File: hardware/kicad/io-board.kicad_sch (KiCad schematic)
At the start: 50 parts, among them J1 NCJ6FI-S, J2 NCJ6FI-S, J3 NCJ6FI-S, J4 NCJ6FI-S, P1 JIO-PWR, P2 JIO-WETSEND, P3 JIO-WETRET, P4 JIO-DRY, P5 Wet/Dry control, P6 Mono switch, U1 OPA1644AIDR, U2 OPA1656IDR, U3 OPA1656IDR, U4 OPA1656IDR

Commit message: Board 6 io-board complete (ERC 0, sim verified, DRC 0/0 with ground grid stitching); all six boards READY TO ORDER; fab packet with gerber zips, BOMs, pos files, ORDER-PACKET.md; readiness report regenerated
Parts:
- removed C1, C2, C3, C4: 220p DNP, Capacitor_SMD:C_0603_1608Metric, symbol Device:C_Small
- removed C91, C92, C93, C94, C95, C96, C97, C98: 100n, Capacitor_SMD:C_0603_1608Metric, symbol Device:C_Small
- removed J1, J2, J3, J4: NCJ6FI-S, Connector_Audio:Jack_XLR-6.35mm_Neutrik_NCJ6FI-V_Vertical, symbol Connector_Audio:NCJ6FI-V
- removed R1, R2, R3, R4: 100R, Resistor_SMD:R_0603_1608Metric, symbol Device:R_Small
- removed R11, R12, R13, R14, R15, R16, R17, R18: 10k 0.1%, Resistor_SMD:R_0603_1608Metric, symbol Device:R_Small
- removed R31, R32, R35, R36: 20k, Resistor_SMD:R_0603_1608Metric, symbol Device:R_Small
- removed R43, R44, R53, R54: 10k, Resistor_SMD:R_0603_1608Metric, symbol Device:R_Small
- removed R49, R50, R59, R60: 49.9R, Resistor_SMD:R_0603_1608Metric, symbol Device:R_Small
- removed U1: OPA1644AIDR, Package_SO:SOIC-14_3.9x8.7mm_P1.27mm, symbol Amplifier_Operational:OPA4134
- added C1, C2, C3, C4: 220p, Capacitor_SMD:C_0805_2012Metric, symbol Device:C
- added C100, C99: 22u, Capacitor_SMD:C_1210_3225Metric, symbol Device:C
- added C91, C92, C93, C94, C95, C96, C97, C98: 100n, Capacitor_SMD:C_0805_2012Metric, symbol Device:C
- added J1: to L IN combo jack, Connector_JST:JST_XH_B3B-XH-A_1x03_P2.50mm_Vertical, symbol Connector_Generic:Conn_01x03
- added J2: to R IN combo jack, Connector_JST:JST_XH_B3B-XH-A_1x03_P2.50mm_Vertical, symbol Connector_Generic:Conn_01x03
- added J3: to L OUT combo jack, Connector_JST:JST_XH_B3B-XH-A_1x03_P2.50mm_Vertical, symbol Connector_Generic:Conn_01x03
- added J4: to R OUT combo jack, Connector_JST:JST_XH_B3B-XH-A_1x03_P2.50mm_Vertical, symbol Connector_Generic:Conn_01x03
- added R1, R2, R21, R22, R23, R24, R3, R4: 100, Resistor_SMD:R_0805_2012Metric, symbol Device:R
- added R11, R12, R13, R14, R15, R16, R17, R18, R43, R44, R53, R54: 10k, Resistor_SMD:R_0805_2012Metric, symbol Device:R
- added R31, R32, R35, R36: 20k, Resistor_SMD:R_0805_2012Metric, symbol Device:R
- added R49, R50, R59, R60: 49.9, Resistor_SMD:R_0805_2012Metric, symbol Device:R
- added U1: OPA1644AIDR, Package_SO:SOIC-14_3.9x8.7mm_P1.27mm, symbol Amplifier_Operational:TL074
- P1: value JIO-PWR -> JIO-PWR B3P-VH-B
- P2: value JIO-WETSEND -> P2
- P3: value JIO-WETRET -> P3
- P4: value JIO-DRY -> P4
- P5: value Wet/Dry control -> P5
- P6: value Mono switch -> P6
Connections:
- net +15VA: now also P1.1 (Pin_1), U2.8 (V+), U3.8 (V+), U4.8 (V+), C91.1, C93.1, C95.1, C97.1, C99.1, U1.4 (V+)
- net -15VA: now also P1.3 (Pin_3), U2.4 (V-), U3.4 (V-), U4.4 (V-), C100.1, C92.1, C94.1, C96.1, C98.1, U1.11 (V-)
- net AGND: now also P1.2 (Pin_2), P2.2 (Pin_2), P3.2 (Pin_2), P4.2 (Pin_2), U2.3 (+), U2.5 (+), U3.5 (+), U4.5 (+), C1.2, C100.2, C2.2, C3.2, C4.2, C91.2, C92.2, C93.2, C94.2, C95.2, C96.2, C97.2, C98.2, C99.2, J1.3 (Pin_3), J2.3 (Pin_3), J3.3 (Pin_3), J4.3 (Pin_3), R14.2, R18.2
- net DRY_L: now also P4.1 (Pin_1), R21.2
- net DRY_R: now also P4.3 (Pin_3), R23.2
- net IN_BAL_L_N: now also C2.1, J1.2 (Pin_2), R2.1
- net IN_BAL_L_P: now also C1.1, J1.1 (Pin_1), R1.1
- net IN_BAL_R_N: now also C4.1, J2.2 (Pin_2), R4.1
- net IN_BAL_R_P: now also C3.1, J2.1 (Pin_1), R3.1
- net L_BLEND: now also U2.1, U3.3 (+), R35.1, R43.1
- net MONO_C: now also P6.2 (Pin_2), U1.12 (+)
- net OUT_BAL_L_N: now also J3.2 (Pin_2), R50.2
- net OUT_BAL_L_P: now also J3.1 (Pin_1), R49.2
- net OUT_BAL_R_N: now also J4.2 (Pin_2), R60.2
- net OUT_BAL_R_P: now also J4.1 (Pin_1), R59.2
- net R_BLEND: now also U2.7, U4.3 (+), R36.1, R53.1
- net WD_L_WIPER: now also P5.2 (Pin_2), R31.1
- net WD_R_WIPER: now also P5.5 (Pin_5), R32.1
- net WET_SEND_L: now also P2.1 (Pin_1), R22.2
- net WET_SEND_R: now also P2.3 (Pin_3), R24.2
- new net L_PROG: P5.1 (Pin_1), R21.1, R22.1, U1.8, U1.9 (-)
- new net L_RX: P6.1 (Pin_1), R12.1, U1.1, U1.10 (+)
- new net N_COLD_L: R44.1, R50.1, U3.7
- new net N_COLD_R: R54.1, R60.1, U4.7
- new net N_HOT_L: R49.1, U3.1, U3.2 (-)
- new net N_HOT_R: R59.1, U4.1, U4.2 (-)
- new net N_INL_N: R11.1, R2.2
- new net N_INL_P: R1.2, R13.1
- new net N_INR_N: R15.1, R4.2
- new net N_INR_P: R17.1, R3.2
- new net N_U1A_M: R11.2, R12.2, U1.2 (-)
- new net N_U1A_P: R13.2, R14.1, U1.3 (+)
- new net N_U1B_M: R15.2, R16.2, U1.6 (-)
- new net N_U1B_P: R17.2, R18.1, U1.5 (+)
- new net N_U2A_M: R31.2, R35.2, U2.2 (-)
- new net N_U2B_M: R32.2, R36.2, U2.6 (-)
- new net N_U3B_M: R43.2, R44.2, U3.6 (-)
- new net N_U4B_M: R53.2, R54.2, U4.6 (-)
- new net R_PROG: P5.4 (Pin_4), R23.1, R24.1, U1.13 (-), U1.14
- new net R_RX: P6.3 (Pin_3), R16.1, U1.7
- new net WET_SUM_L: P3.1 (Pin_1), P5.3 (Pin_3)
- new net WET_SUM_R: P3.3 (Pin_3), P5.6 (Pin_6)
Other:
- note added: "BALANCED OUTPUT DRIVERS (+4dBu, 600R-capable)"
- note added: "BALANCED RECEIVERS (unity differential)"
- note added: "HEADERS"
- note added: "MONO ROUTING + PROGRAM BUFFERS + FANOUT"
- note added: "PANEL JACK LANDINGS (NCJ6FI-S combo jacks, hand-wired)"
- note added: "POWER + DECOUPLING"
- note added: "WET/DRY BLEND BUFFERS"
- title: GAS Rev A - Input Output Board -> GAS Rev A - Input Output Board Board

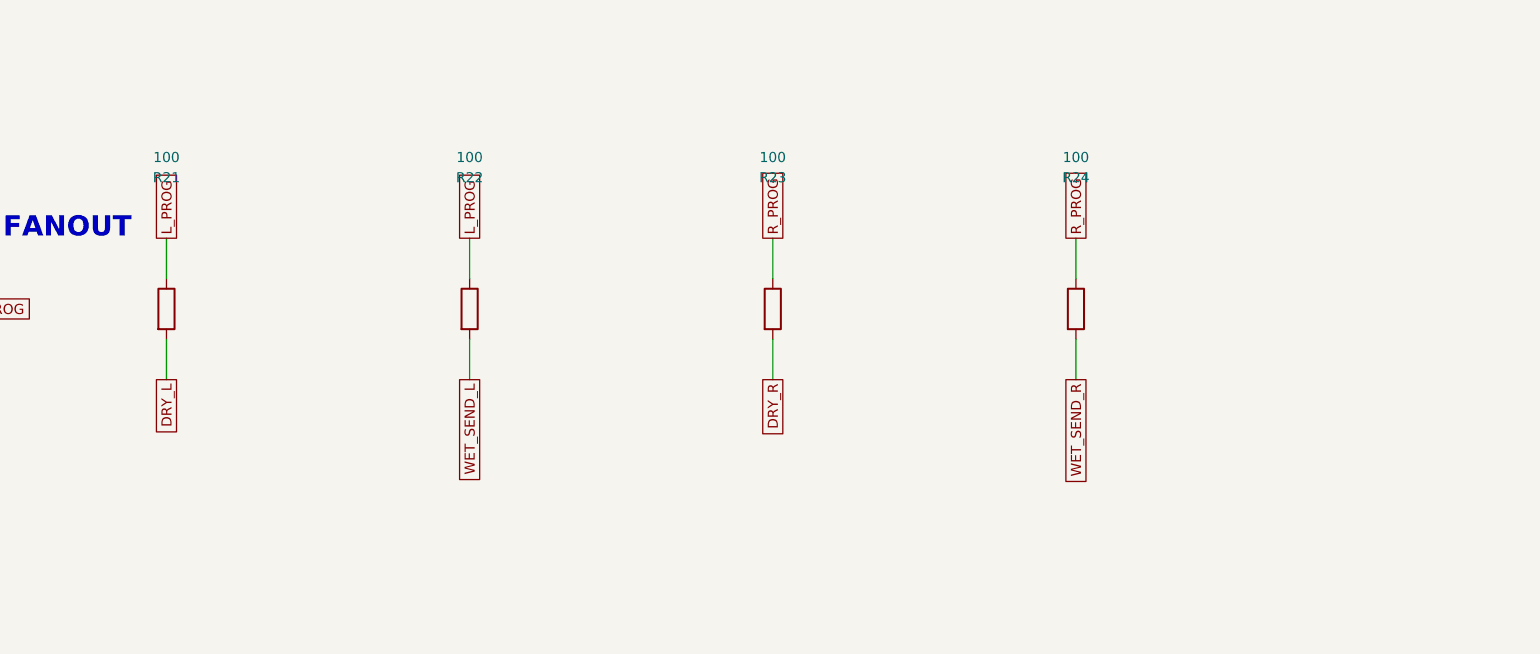
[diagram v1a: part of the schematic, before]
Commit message: Schematic review (kicad-schematic-review skill): F1 R-78E moved to +15VRAW, F2 mono-float bleed R25; both boards re-routed/verified; datasheet cache, per-instance reviews, schematic_review.md
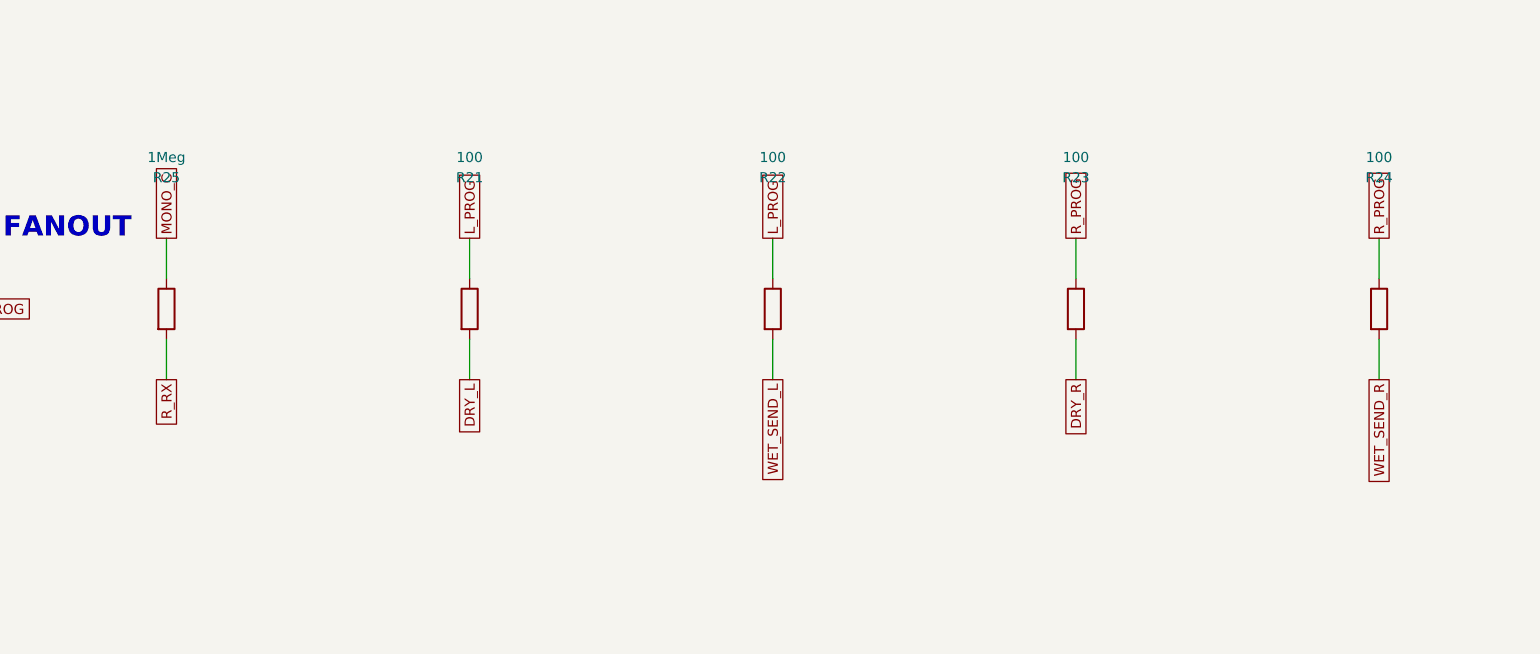
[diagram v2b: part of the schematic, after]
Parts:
- removed R31, R32: 20k, Resistor_SMD:R_0805_2012Metric, symbol Device:R
- removed R43, R53: 10k, Resistor_SMD:R_0805_2012Metric, symbol Device:R
- removed R49, R59: 49.9, Resistor_SMD:R_0805_2012Metric, symbol Device:R
- removed unit 5 of U1
- added C100: 22u, Capacitor_SMD:C_1210_3225Metric, symbol Device:C
- added R24: 100, Resistor_SMD:R_0805_2012Metric, symbol Device:R
- added R36: 20k, Resistor_SMD:R_0805_2012Metric, symbol Device:R
- added R60: 49.9, Resistor_SMD:R_0805_2012Metric, symbol Device:R
- added unit 2 of U2
- added unit 2 of U3
- added unit 1 of U4
- added unit 2 of U4
- C98: renamed from C99; value 22u -> 100n; footprint Capacitor_SMD:C_1210_3225Metric -> Capacitor_SMD:C_0805_2012Metric
- R25: renamed from R21; value 100 -> 1Meg
- R35: renamed from U2; value OPA1656IDR -> 20k; footprint Package_SO:SOIC-8_3.9x4.9mm_P1.27mm -> Resistor_SMD:R_0805_2012Metric; symbol Amplifier_Operational:OPA1656ID -> Device:R
- R44: renamed from R50; value 49.9 -> 10k
- R49: renamed from U3; value OPA1656IDR -> 49.9; footprint Package_SO:SOIC-8_3.9x4.9mm_P1.27mm -> Resistor_SMD:R_0805_2012Metric; symbol Amplifier_Operational:OPA1656ID -> Device:R
- R50, R59: renamed from U4; value OPA1656IDR -> 49.9; footprint Package_SO:SOIC-8_3.9x4.9mm_P1.27mm -> Resistor_SMD:R_0805_2012Metric; symbol Amplifier_Operational:OPA1656ID -> Device:R
- R54: renamed from R60; value 49.9 -> 10k
- U1: renamed from U2; value OPA1656IDR -> OPA1644AIDR; footprint Package_SO:SOIC-8_3.9x4.9mm_P1.27mm -> Package_SO:SOIC-14_3.9x8.7mm_P1.27mm; symbol Amplifier_Operational:OPA1656ID -> Amplifier_Operational:TL074
- U4: renamed from C91; value 100n -> OPA1656IDR; footprint Capacitor_SMD:C_0805_2012Metric -> Package_SO:SOIC-8_3.9x4.9mm_P1.27mm; symbol Device:C -> Amplifier_Operational:OPA1656ID
- renumbered C92 to C91, C93 to C92, C94 to C93, C95 to C94, C96 to C95, C97 to C96, C98 to C97, C100 to C99, R22 to R21, R23 to R22, R24 to R23, R35 to R31, R36 to R32, R44 to R43, R54 to R53, U3 to U2, U4 to U3
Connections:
- net +15VA: now also C91.1, C93.1, C95.1, C97.1, C99.1, U1.4 (V+), U4.8 (V+); no longer C92.1, C94.1, C96.1, C98.1, U1.8 (V+), U4.1
- net -15VA: now also C92.1, C94.1, C96.1, C98.1, U1.11 (V-), U4.4 (V-), C100.1; no longer C91.1, C93.1, C95.1, C97.1, C99.1, U1.4 (V-)
- net AGND: now also C100.2, U2.5 (+), U3.5 (+), U4.5 (+); no longer R35.5 (+), R49.5 (+), R59.5 (+), U4.2
- net DRY_L: now also R21.2; no longer R25.2
- net DRY_R: now also R23.2; no longer R22.2
- net L_BLEND: now also R35.1, R43.1; no longer R31.1
- net L_PROG: now also R22.1; no longer R25.1
- net MONO_C: now also R25.1
- net N_COLD_L: now also R50.1, U3.7; no longer R43.1, R49.7
- net N_COLD_R: now also R60.1, U4.7; no longer R53.1, R59.7
- net N_HOT_L: now also R49.1
- net N_HOT_R: now also R59.1, U4.1, U4.2 (-); no longer R50.1, R50.2 (-)
- net N_U2A_M: now also R35.2
- net N_U2B_M: now also R36.2, U2.6 (-); no longer R35.6 (-)
- net N_U3B_M: now also R44.2, U3.6 (-); no longer R49.6 (-)
- net N_U4B_M: now also R54.2, U4.6 (-); no longer R59.6 (-)
- net OUT_BAL_L_N: now also R50.2; no longer R44.2
- net OUT_BAL_L_P: now also R49.2
- net OUT_BAL_R_N: now also R60.2; no longer R54.2
- net OUT_BAL_R_P: now also R59.2
- net R_BLEND: now also R53.1, R36.1, U2.7, U4.3 (+); no longer R32.1, R35.7, R50.3 (+)
- net R_PROG: now also R24.1; no longer R22.1
- net R_RX: now also R25.2
- net WD_L_WIPER: now also R31.1
- net WD_R_WIPER: now also R32.1
- net WET_SEND_L: now also R22.2; no longer R21.2
- net WET_SEND_R: now also R24.2; no longer R23.2
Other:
- moved on the sheet: C91, C92, C93, C94, C95, C96, C97, C98, C99, R31, R32, R43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
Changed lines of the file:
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@@
 	(wire
 		(pts
+			(xy 279.40 341.63) (xy 279.40 336.55)
+		)
+		(stroke
+			(width 0)
+			(type default)
+		)
+	)
+	(wire
+		(pts
+			(xy 279.40 349.25) (xy 279.40 354.33)
+		)
+		(stroke
+			(width 0)
+			(type default)
+		)
+	)
+	(wire
+		(pts
 			(xy 58.42 416.56) (xy 63.50 416.56)
 		)
@@
 		)
 	)
-	(global_label "L_PROG"
+	(global_label "MONO_C"
 		(shape passive)
 		(at 127.00 336.55 90)
@@
 		)
 	)
-	(global_label "DRY_L"
+	(global_label "R_RX"
 		(shape passive)
 		(at 127.00 354.33 270)
@@
 		)
 	)
-	(global_label "WET_SEND_L"
+	(global_label "DRY_L"
 		(shape passive)
 		(at 165.10 354.33 270)
@@
 		)
 	)
-	(global_label "R_PROG"
+	(global_label "L_PROG"
 		(shape passive)
 		(at 203.20 336.55 90)
@@
 		)
 	)
-	(global_label "DRY_R"
+	(global_label "WET_SEND_L"
 		(shape passive)
 		(at 203.20 354.33 270)
@@
 		)
 	)
-	(global_label "WET_SEND_R"
+	(global_label "DRY_R"
 		(shape passive)
 		(at 241.30 354.33 270)
@@
 		)
 	)
+	(global_label "R_PROG"
+		(shape passive)
+		(at 279.40 336.55 90)
+		(fields_autoplaced yes)
+		(effects
+			(font
+				(size 1.27 1.27)
+			)
+			(justify left)
+		)
+		(property "Intersheetrefs" "${INTERSHEET_REFS}"
+			(at 279.40 336.55 0)
+			(effects
+				(font
+					(size 1.27 1.27)
+				)
+				(hide yes)
+			)
+		)
+	)
+	(global_label "WET_SEND_R"
+		(shape passive)
+		(at 279.40 354.33 270)
+		(fields_autoplaced yes)
+		(effects
+			(font
+				(size 1.27 1.27)
+			)
+			(justify right)
+		)
+		(property "Intersheetrefs" "${INTERSHEET_REFS}"
+			(at 279.40 354.33 0)
+			(effects
+				(font
+					(size 1.27 1.27)
+				)
+				(hide yes)
+			)
+		)
+	)
 	(global_label "L_BLEND"
 		(shape passive)
@@
 		(dnp no)
 		(fields_autoplaced yes)
-		(property "Reference" "R21"
+		(property "Reference" "R25"
 			(at 127.00 328.93 0)
 			(effects
@@
 			)
 		)
-		(property "Value" "100"
+		(property "Value" "1Meg"
 			(at 127.00 326.39 0)
 			(effects
@@
 			(project "io-board"
 				(path "/afb0f8c4-bf37-5c17-978a-b0f2cc7e01bd"
-					(reference "R21")
+					(reference "R25")
 					(unit 1)
 				)
@@
 		(dnp no)
 		(fields_autoplaced yes)
-		(property "Reference" "R22"
+		(property "Reference" "R21"
 			(at 165.10 328.93 0)
 			(effects
@@
 			(project "io-board"
 				(path "/afb0f8c4-bf37-5c17-978a-b0f2cc7e01bd"
-					(reference "R22")
+					(reference "R21")
 					(unit 1)
 				)
@@
 		(dnp no)
 		(fields_autoplaced yes)
-		(property "Reference" "R23"
+		(property "Reference" "R22"
 			(at 203.20 328.93 0)
 			(effects
@@
 			(project "io-board"
 				(path "/afb0f8c4-bf37-5c17-978a-b0f2cc7e01bd"
-					(reference "R23")
+					(reference "R22")
 					(unit 1)
 				)
@@
 		(dnp no)
 		(fields_autoplaced yes)
-		(property "Reference" "R24"
+		(property "Reference" "R23"
 			(at 241.30 328.93 0)
 			(effects
@@
 			(effects
 				(font
+					(size 1.27 1.27)
+				)
+				(hide yes)
+			)
+		)
+		(pin "1"
+		)
+		(pin "2"
+		)
+		(instances
+			(project "io-board"
+				(path "/afb0f8c4-bf37-5c17-978a-b0f2cc7e01bd"
+					(reference "R23")
+					(unit 1)
+				)
+			)
+		)
+	)
+	(symbol
+		(lib_id "Device:R")
+		(at 279.40 345.44 0)
+		(unit 1)
+		(exclude_from_sim no)
+		(in_bom yes)
+		(on_board yes)
+		(dnp no)
+		(fields_autoplaced yes)
+		(property "Reference" "R24"
+			(at 279.40 328.93 0)
+			(effects
+				(font
+					(size 1.27 1.27)
+				)
+			)
+		)
+		(property "Value" "100"
+			(at 279.40 326.39 0)
+			(effects
+				(font
+					(size 1.27 1.27)
+				)
+			)
+		)
+		(property "Footprint" "Resistor_SMD:R_0805_2012Metric"
+			(at 279.40 323.85 0)
+			(effects
+				(font
+					(size 1.27 1.27)
+				)
+				(hide yes)
+			)
+		)
+		(property "Datasheet" ""
+			(at 279.40 321.31 0)
+			(effects
+				(font
